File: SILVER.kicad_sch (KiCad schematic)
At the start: 2 parts, among them J1 Conn_02x22, J2 Conn_02x22

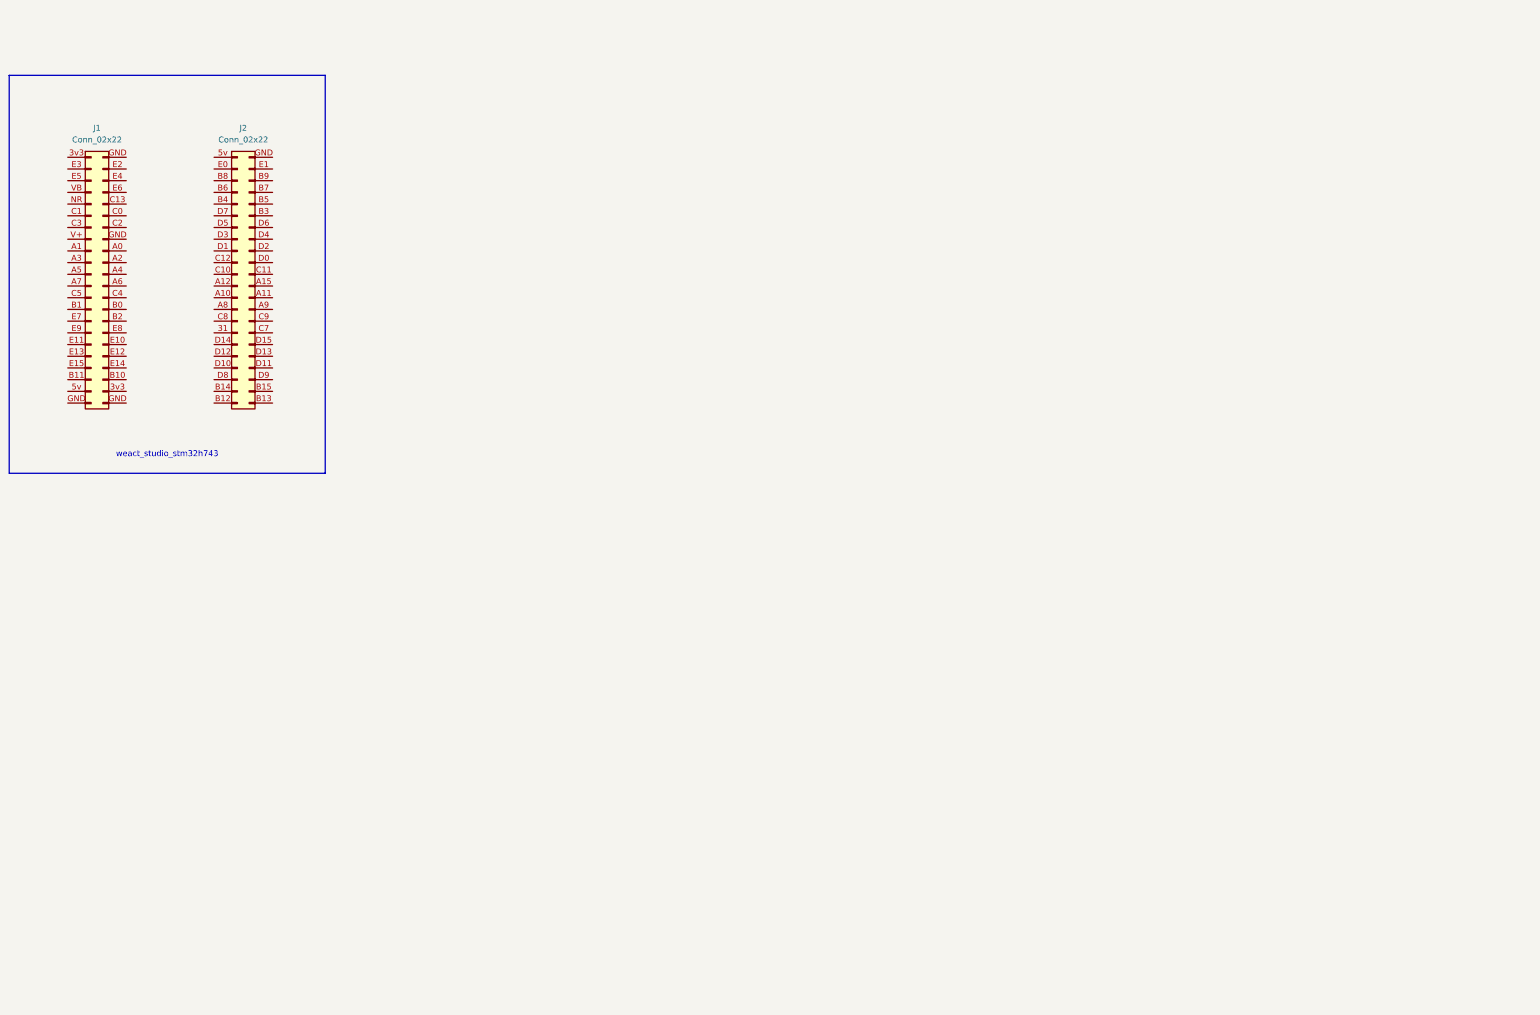
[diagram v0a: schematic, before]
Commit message: feat: Add new dc-dc converter and VNH5019 motor driver projects, update main schematic with motor connectors.
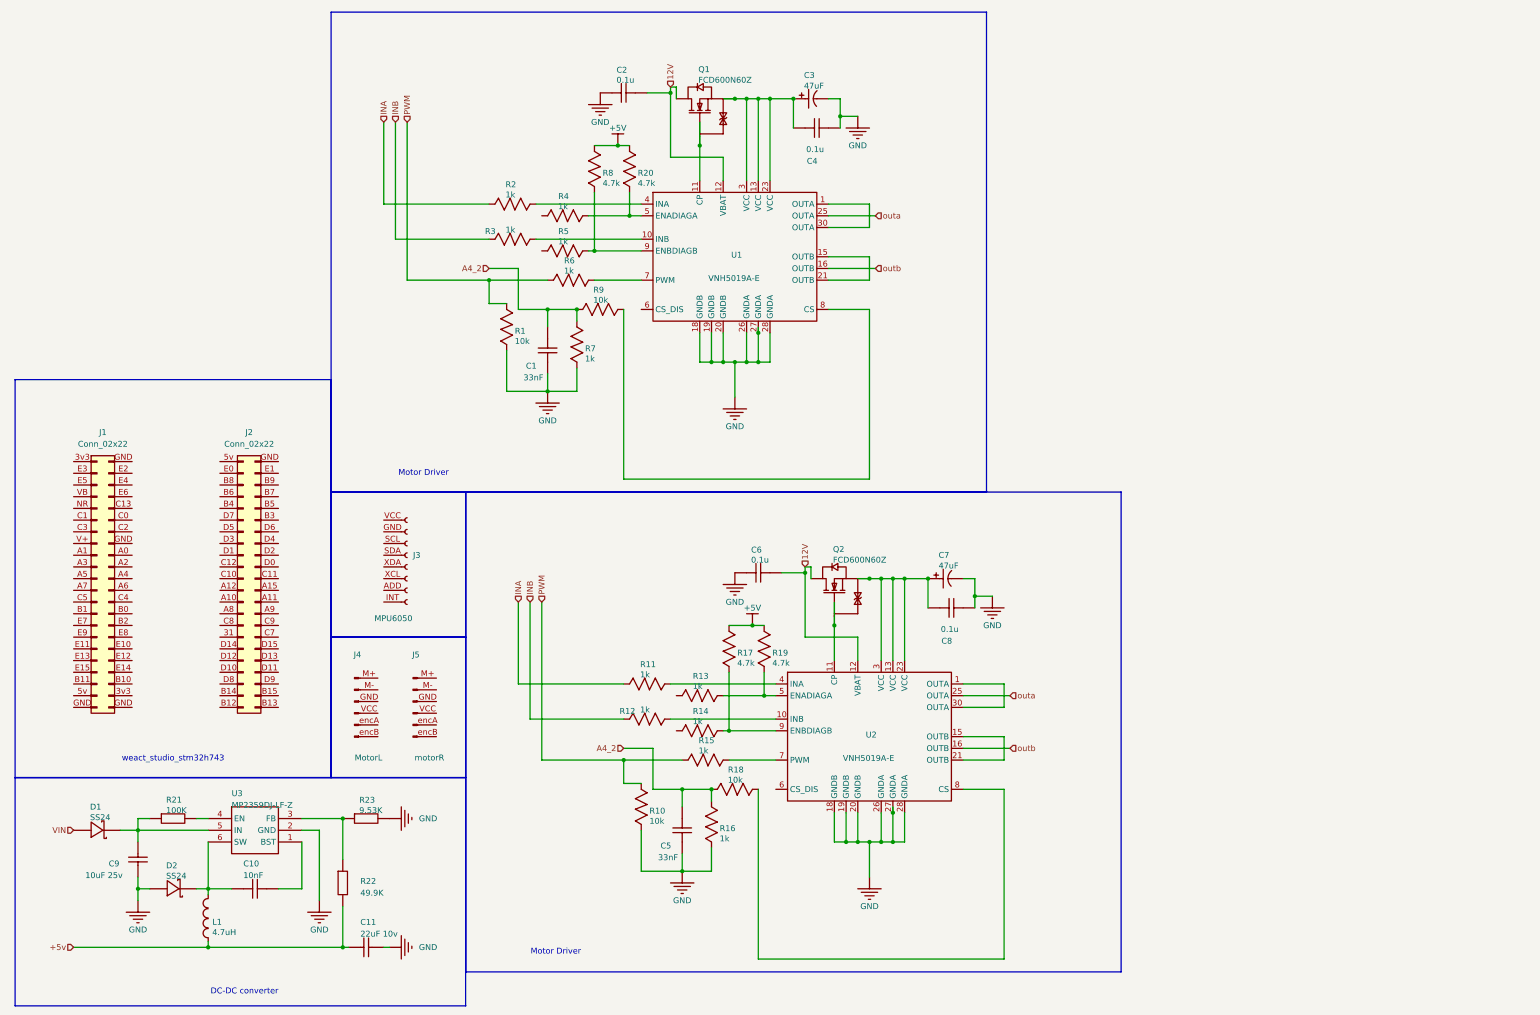
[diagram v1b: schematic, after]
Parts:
- added C1, C5: 33nF, Capacitor_SMD:C_0805_2012Metric, symbol VNH5019-altium-import:root_3_33nF_
- added C10: 10nF, Capacitor_SMD:C_0805_2012Metric, symbol dc-dc converter-altium-import:root_0_10nF_
- added C11: 22uF 10v, Capacitor_SMD:C_0805_2012Metric, symbol dc-dc converter-altium-import:root_2_22uF 10v_
- added C2, C4, C6, C8: 0.1u, Capacitor_SMD:C_0805_2012Metric, symbol VNH5019-altium-import:root_0_0.1u_
- added C3, C7: 47uF, Capacitor_SMD:C_Elec_6.3x5.4, symbol VNH5019-altium-import:root_0_47uF_
- added C9: 10uF 25v, Capacitor_SMD:C_0805_2012Metric, symbol dc-dc converter-altium-import:root_3_10uF 25v_
- added D1, D2: SS24, Diode_SMD:D_SMA, symbol dc-dc converter-altium-import:root_0_SS24_
- added J3: MPU6050, Connector_PinSocket_2.54mm:PinSocket_1x08_P2.54mm_Vertical, symbol Connector:Conn_01x08_Socket
- added J4: MotorL, Connector_PinHeader_2.54mm:PinHeader_1x06_P2.54mm_Vertical, symbol Connector:Conn_01x06_Pin
- added J5: motorR, Connector_PinHeader_2.54mm:PinHeader_1x06_P2.54mm_Vertical, symbol Connector:Conn_01x06_Pin
- added L1: 4.7uH, Library:IND_5028_TDK, symbol dc-dc converter-altium-import:root_1_4.7uH_
- added Q1, Q2: FCD600N60Z, Package_TO_SOT_SMD:TO-252-2, symbol VNH5019-altium-import:root_1_FCD600N60Z_
- added R1, R10: 10k, Resistor_SMD:R_0508_1220Metric, symbol VNH5019-altium-import:root_1_10k_
- added R11, R12, R13, R14, R15, R2, R3, R4, R5, R6: 1k, Resistor_SMD:R_0508_1220Metric, symbol VNH5019-altium-import:root_0_1k_
- added R16, R7: 1k, Resistor_SMD:R_0508_1220Metric, symbol VNH5019-altium-import:root_1_1k_
- added R17, R19, R20, R8: 4.7k, Resistor_SMD:R_0508_1220Metric, symbol VNH5019-altium-import:root_1_4.7k_
- added R18, R9: 10k, Resistor_SMD:R_0508_1220Metric, symbol VNH5019-altium-import:root_0_10k_
- added R21: 100K, Resistor_SMD:R_0508_1220Metric, symbol dc-dc converter-altium-import:root_0_100K_
- added R22: 49.9K, Resistor_SMD:R_0508_1220Metric, symbol dc-dc converter-altium-import:root_1_49.9K_
- added R23: 9.53K, Resistor_SMD:R_0508_1220Metric, symbol dc-dc converter-altium-import:root_2_9.53K_
- added U1, U2: VNH5019A-E, Package_SO:ST_MultiPowerSO-30, symbol VNH5019-altium-import:root_0_VNH5019A-E_
- added U3: MP2359DJ-LF-Z, Package_TO_SOT_SMD:SOT-23-6, symbol dc-dc converter-altium-import:root_2_MP2359DJ-LF-Z_
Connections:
- new net: R20.1, R4.2, U1.5 (ENADIAGA)
- new net: C9.1, D1.2 (K), R21.1, U3.5 (IN)
- new net: R22.2, R23.2, U3.3 (FB)
- new net: C10.1, D2.2 (K), L1.2, U3.6 (SW)
- new net: C10.2, U3.1 (BST)
- new net: R18.2, U2.8 (CS)
- new net: C7.1, C8.1, Q2.3 (S), U2.13 (VCC), U2.23 (VCC), U2.3 (VCC)
- new net: C3.1, C4.1, Q1.3 (S), U1.13 (VCC), U1.23 (VCC), U1.3 (VCC)
- new net: R6.2, U1.7 (PWM)
- new net: Q2.1 (G), U2.11 (CP)
- new net: R2.2, U1.4 (INA)
- new net: R9.2, U1.8 (CS)
- new net: R3.2, U1.10 (INB)
- new net: R21.2, U3.4 (EN)
- new net: R11.2, U2.4 (INA)
- new net: R14.2, R17.1, U2.9 (ENBDIAGB)
- new net: Q1.1 (G), U1.11 (CP)
- new net: R5.2, R8.1, U1.9 (ENBDIAGB)
- new net: R13.2, R19.1, U2.5 (ENADIAGA)
- new net: R15.2, U2.7 (PWM)
- new net: U2.1 (OUTA), U2.30 (OUTA)
- new net: R12.2, U2.10 (INB)
- new net: U2.15 (OUTB), U2.21 (OUTB)
- new net: U1.1 (OUTA), U1.30 (OUTA)
- new net: U1.15 (OUTB), U1.21 (OUTB)
- new net +5V: R17.2, R19.2, R20.2, R8.2
- new net +5v: C11.2, L1.1, R22.1
- new net 12V: C2.2, C6.2, Q1.4 (D), Q2.4 (D), U1.12 (VBAT), U2.12 (VBAT)
- new net A4_2: C1.1, C5.1, R16.2, R18.1, R7.2, R9.1
- new net GND: C1.2, C11.1, C2.1, C3.2, C4.2, C5.2, C6.1, C7.2, C8.2, C9.2, D2.1 (A), R1.1, R10.1, R16.1, R23.1, R7.1, U1.18 (GNDB), U1.19 (GNDB), U1.20 (GNDB), U1.26 (GNDA), U1.27 (GNDA), U1.28 (GNDA), U2.18 (GNDB), U2.19 (GNDB), U2.20 (GNDB), U2.26 (GNDA), U2.27 (GNDA), U2.28 (GNDA), U3.2 (GND)
- new net INA: R11.1, R2.1
- new net INB: R12.1, R3.1
- new net PWM: R1.2, R10.2, R15.1, R6.1
- new net VIN: D1.1 (A)
- new net outa: U1.25 (OUTA), U2.25 (OUTA)
- new net outb: U1.16 (OUTB), U2.16 (OUTB)
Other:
- note added: "DC-DC converter"
- note added: "Motor Driver"
- moved on the sheet: J1, J2

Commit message: feat: Introduce LM2596 and STLINK KiCad projects with new symbols and footprints, and update the main SILVER project.
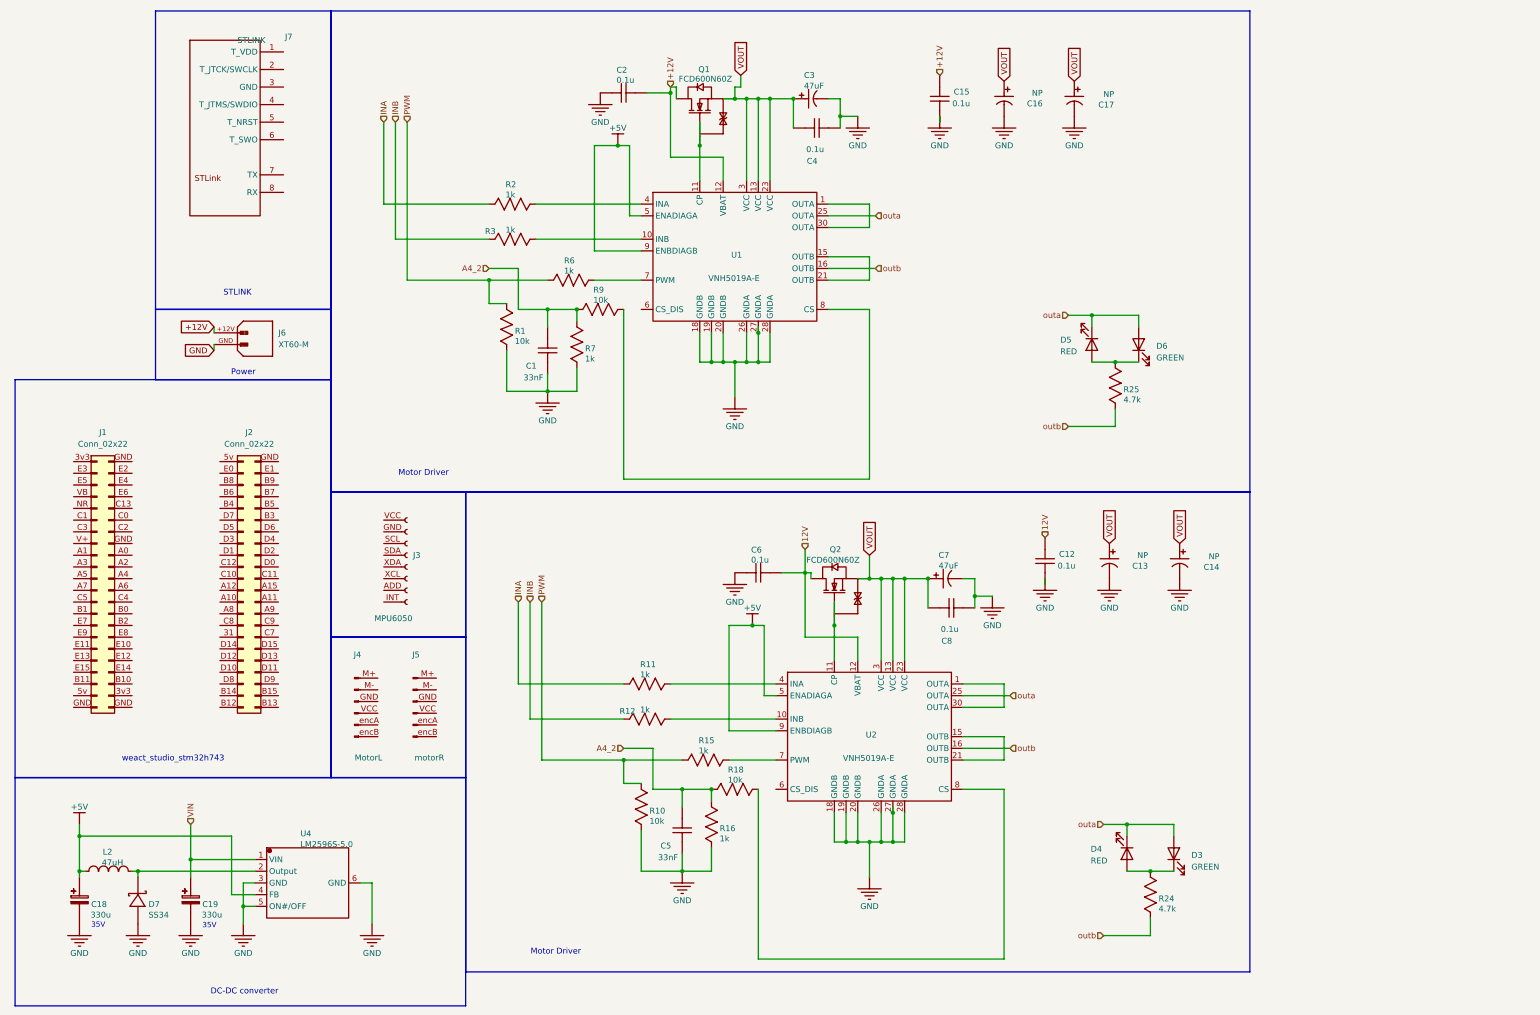
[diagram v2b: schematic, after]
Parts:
- removed C10: 10nF, Capacitor_SMD:C_0805_2012Metric, symbol dc-dc converter-altium-import:root_0_10nF_
- removed C11: 22uF 10v, Capacitor_SMD:C_0805_2012Metric, symbol dc-dc converter-altium-import:root_2_22uF 10v_
- removed C9: 10uF 25v, Capacitor_SMD:C_0805_2012Metric, symbol dc-dc converter-altium-import:root_3_10uF 25v_
- removed D1, D2: SS24, Diode_SMD:D_SMA, symbol dc-dc converter-altium-import:root_0_SS24_
- removed L1: 4.7uH, Library:IND_5028_TDK, symbol dc-dc converter-altium-import:root_1_4.7uH_
- removed R13, R14, R4, R5: 1k, Resistor_SMD:R_0508_1220Metric, symbol VNH5019-altium-import:root_0_1k_
- removed R17, R19, R20, R8: 4.7k, Resistor_SMD:R_0508_1220Metric, symbol VNH5019-altium-import:root_1_4.7k_
- removed R21: 100K, Resistor_SMD:R_0508_1220Metric, symbol dc-dc converter-altium-import:root_0_100K_
- removed R22: 49.9K, Resistor_SMD:R_0508_1220Metric, symbol dc-dc converter-altium-import:root_1_49.9K_
- removed R23: 9.53K, Resistor_SMD:R_0508_1220Metric, symbol dc-dc converter-altium-import:root_2_9.53K_
- removed U3: MP2359DJ-LF-Z, Package_TO_SOT_SMD:SOT-23-6, symbol dc-dc converter-altium-import:root_2_MP2359DJ-LF-Z_
- added C12, C15: 0.1u, Capacitor_SMD:C_0805_2012Metric, symbol VNH5019-altium-import:root_0_0.1u_
- added C13, C14, C16, C17: NP, Capacitor_SMD:C_Elec_6.3x5.4, symbol VNH5019-altium-import:root_0_47uF_
- added C18, C19: 330u, Capacitor_SMD:CP_Elec_8x10.5, symbol LM2596-altium-import:root_0_330u_
- added D3, D6: GREEN, LED_SMD:LED_0603_1608Metric, symbol Device:LED
- added D4, D5: RED, LED_SMD:LED_0603_1608Metric, symbol Device:LED
- added D7: SS34, Diode_SMD:D_SMA, symbol LM2596-altium-import:root_1_SS34_
- added J6: XT60-M, Connector_AMASS:AMASS_XT60-M_1x02_P7.20mm_Vertical, symbol weact_studio_stm32h743_1:XT60-M
- added J7: STLINK, Library:STLINK, symbol STLINK-altium-import:root_0_NUCLEO-F401-STLINKEXTRACT_
- added L2: 47uH, Inductor_SMD:L_12x12mm_H6mm, symbol LM2596-altium-import:root_0_47uH_
- added R24, R25: 4.7k, Resistor_SMD:R_0508_1220Metric, symbol VNH5019-altium-import:root_1_4.7k_
- added U4: LM2596S-5.0, Package_TO_SOT_SMD:TO-263-5_TabPin3, symbol LM2596-altium-import:root_0_LM2596S-5.0_
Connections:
- net +5V: now also U1.5 (ENADIAGA), U1.9 (ENBDIAGB), U2.5 (ENADIAGA), U2.9 (ENBDIAGB), C18.1, L2.1, U4.4 (FB)
- net 12V: now also C12.1; no longer C2.2, Q1.4 (D), U1.12 (VBAT)
- net GND: now also C12.2, C13.2, C14.2, C15.2, C16.2, C17.2, C18.2, C19.2, D7.1 (A), J6.GND (-), U4.3 (GND), U4.5 (ON#/OFF), U4.6 (GND)
- net VIN: now also C19.1, U4.1 (VIN)
- net outa: now also D3.2 (A), D4.1 (K), D5.1 (K), D6.2 (A)
- net outb: now also R24.1, R25.1
- net VOUT: now reaches C7.1, C8.1, Q2.3 (S), U2.13 (VCC), U2.23 (VCC), U2.3 (VCC)
- net VOUT: now also C3.1, C4.1, Q1.3 (S), U1.13 (VCC), U1.23 (VCC), U1.3 (VCC), C13.1, C14.1, C16.1, C17.1
- new net: D7.2 (K), L2.2, U4.2 (Output)
- new net: D3.1 (K), D4.2 (A), R24.2
- new net: D5.2 (A), D6.1 (K), R25.2
- new net +12V: C15.1, C2.2, J6.+12V (+), Q1.4 (D), U1.12 (VBAT)
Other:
- note added: "35V"
- note added: "Power"
- note added: "STLINK"

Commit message: feat: Update main project schematic and PCB with new component footprint and connector details, and add new RB141C1100 component files.
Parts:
- removed J1, J2: Conn_02x22, Connector_PinSocket_2.54mm:PinSocket_2x22_P2.54mm_Vertical, symbol Connector_Generic_MountingPin:Conn_02x22_Odd_Even_MountingPin
- added J1: Conn_01x13, Connector_FFC-FPC:Hirose_FH12-13S-0.5SH_1x13-1MP_P0.50mm_Horizontal, symbol Connector:Conn_01x13_Socket
- added J10, J9: Conn_02x22_Odd_Even_MountingPin, Connector_PinSocket_2.54mm:PinSocket_2x22_P2.54mm_Vertical, symbol Connector_Generic_MountingPin:Conn_02x22_Odd_Even_MountingPin
- added J8: Conn_01x04_Pin, Connector_PinSocket_2.54mm:PinSocket_1x04_P2.54mm_Vertical, symbol Connector:Conn_01x04_Pin
- added SW1: SW_DIP_x01, Library:SW_RB141C1100, symbol Switch:SW_DIP_x01
- J5: value motorR -> MotorR
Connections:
- net VIN is gone; now on net +12V: C19.1, U4.1 (VIN)
- net +12V: now also C12.1, C6.2, Q1.2 (D), Q2.2 (D), U2.12 (VBAT), SW1.1; no longer J6.+12V (+), Q1.4 (D)
- net +5V: now also J10.2 (Pin_2), J9.42 (Pin_42)
- net GND: now also J3.2 (Pin_2), J4.3 (Pin_3), J5.3 (Pin_3), J6.1 (-), J7.203 (GND), J1.13 (Pin_13), J10.1 (Pin_1), J8.1 (Pin_1), J9.1 (Pin_1), J9.15 (Pin_15), J9.43 (Pin_43), J9.44 (Pin_44); no longer J6.GND (-), U4.6 (GND)
- net CS_DIS_L: now reaches U2.6 (CS_DIS)
- net CS_DIS_R: now reaches U1.6 (CS_DIS)
- removed net 12V: C12.1, C6.2, Q2.4 (D), U2.12 (VBAT)
- net A4_2 renamed CS_L
- net CS_L: no longer C1.1, R7.2, R9.1
- net INA renamed D11
- net D11: now also J10.37 (Pin_37); no longer R2.1
- net INB renamed D10
- net D10: now also J10.38 (Pin_38); no longer R3.1
- net PWM renamed D12
- net D12: now also J10.36 (Pin_36); no longer R1.2, R6.1
- net outa renamed OUTA_L
- net OUTA_L: now also J4.1 (Pin_1); no longer D5.1 (K), D6.2 (A), U1.25 (OUTA)
- net outb renamed OUTB_L
- net OUTB_L: now also J4.2 (Pin_2); no longer R25.1, U1.16 (OUTB)
- new net: J6.2 (+), SW1.2
- new net +3.3V: J1.12 (Pin_12), J3.1 (Pin_1), J4.4 (Pin_4), J5.4 (Pin_4), J7.201 (T_VDD), J8.4 (Pin_4), J9.2 (Pin_2), J9.41 (Pin_41)
- new net A0: J1.3 (Pin_3), J9.17 (Pin_17)
- new net A1: J1.4 (Pin_4), J9.18 (Pin_18)
- new net A10: J10.26 (Pin_26)
- new net A11: J10.25 (Pin_25)
- new net A12: J10.24 (Pin_24)
- new net A15: J10.23 (Pin_23)
- new net A2: J9.19 (Pin_19)
- new net A3: J9.20 (Pin_20)
- new net A4: J1.5 (Pin_5), J9.21 (Pin_21)
- new net A5: J9.22 (Pin_22)
- new net A6: J1.6 (Pin_6), J9.23 (Pin_23)
- new net A7: J1.7 (Pin_7), J9.24 (Pin_24)
- new net A8: J10.28 (Pin_28)
- new net A9: J10.27 (Pin_27)
- new net ADD: J3.7 (Pin_7)
- new net B0: J1.10 (Pin_10), J9.27 (Pin_27)
- new net B1: J1.11 (Pin_11), J9.28 (Pin_28)
- new net B10: J9.39 (Pin_39)
- new net B11: J9.40 (Pin_40)
- new net B12: J10.44 (Pin_44)
- new net B13: J10.43 (Pin_43)
- new net B14: J10.42 (Pin_42)
- new net B15: J10.41 (Pin_41)
- new net B2: J9.29 (Pin_29)
- new net B3: J10.11 (Pin_11)
- new net B4: J10.10 (Pin_10), J4.5 (Pin_5)
- new net B5: J10.9 (Pin_9), J4.6 (Pin_6)
- new net B6: J10.8 (Pin_8), J3.3 (Pin_3)
- new net B7: J10.7 (Pin_7), J3.4 (Pin_4)
- new net B8: J10.6 (Pin_6)
- new net B9: J10.5 (Pin_5)
- new net C0: J1.1 (Pin_1), J9.11 (Pin_11)
- new net C1: J1.2 (Pin_2), J9.12 (Pin_12)
- new net C10: J10.22 (Pin_22)
- new net C11: J10.21 (Pin_21)
- new net C12: J10.20 (Pin_20)
- new net C13: J9.9 (Pin_9)
- new net C2: J9.13 (Pin_13)
- new net C3: J9.14 (Pin_14)
- new net C4: J1.8 (Pin_8), J9.25 (Pin_25)
- new net C5: J1.9 (Pin_9), J9.26 (Pin_26)
- new net C6: J10.32 (Pin_32), J5.6 (Pin_6)
- new net C7: J10.31 (Pin_31), J5.5 (Pin_5)
- new net C8: J10.30 (Pin_30)
- new net C9: J10.29 (Pin_29)
- new net CS_R: C1.1, R7.2, R9.1
- new net D0: J10.19 (Pin_19)
- new net D1: J10.18 (Pin_18)
- new net D13: J10.35 (Pin_35), R1.2, R6.1
- new net D14: J10.34 (Pin_34)
- new net D15: J10.33 (Pin_33)
- new net D2: J10.17 (Pin_17)
- new net D3: J10.16 (Pin_16)
- new net D4: J10.15 (Pin_15)
- new net D5: J10.14 (Pin_14)
- new net D6: J10.13 (Pin_13)
- new net D7: J10.12 (Pin_12)
- new net D8: J10.40 (Pin_40), R3.1
- new net D9: J10.39 (Pin_39), R2.1
- new net E0: J10.4 (Pin_4)
- new net E1: J10.3 (Pin_3)
- new net E10: J9.33 (Pin_33)
- new net E11: J9.34 (Pin_34)
- new net E12: J9.35 (Pin_35)
- new net E13: J9.36 (Pin_36)
- new net E14: J9.37 (Pin_37)
- new net E15: J9.38 (Pin_38)
- new net E2: J9.3 (Pin_3)
- new net E3: J9.4 (Pin_4)
- new net E4: J9.5 (Pin_5)
- new net E5: J9.6 (Pin_6)
- new net E6: J9.7 (Pin_7)
- new net E7: J9.30 (Pin_30)
- new net E8: J9.31 (Pin_31)
- new net E9: J9.32 (Pin_32)
- new net INT: J3.8 (Pin_8)
- new net NR: J7.205 (T_NRST), J9.10 (Pin_10)
- new net OUTA_R: D5.1 (K), D6.2 (A), J5.1 (Pin_1), U1.25 (OUTA)
- new net OUTB_R: J5.2 (M-), R25.1, U1.16 (OUTB)
- new net RX: J7.208 (RX)
- new net SWCLK: J7.202 (T_JTCK/SWCLK), J8.2 (Pin_2)
- new net SWDIO: J7.204 (T_JTMS/SWDIO), J8.3 (Pin_3)
- new net SWO: J7.206 (T_SWO)
- new net TX: J7.207 (TX)
- new net V+: J9.16 (Pin_16)
- new net VB: J9.8 (Pin_8)
- new net XCL: J3.6 (Pin_6)
- new net XDA: J3.5 (Pin_5)
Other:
- note added: "Motor Driver Left"
- note added: "Motor Driver Right"
- note added: "Sensors ribbon flex connector"
- note removed: "Motor Driver"
- moved on the sheet: J3, J4, J5
